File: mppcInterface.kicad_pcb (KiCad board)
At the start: 2 copper layers, 65 x 56.5 mm, 110 parts, among them J1 Conn_Coaxial, J2 Conn_Coaxial, J3 Conn_Coaxial, J4 Conn_Coaxial, J5 Conn_Coaxial, J6 Conn_Coaxial, J7 Conn_Coaxial, J8 Conn_Coaxial, J9 Raspberry_Pi_2_3, Q1 BSS123L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

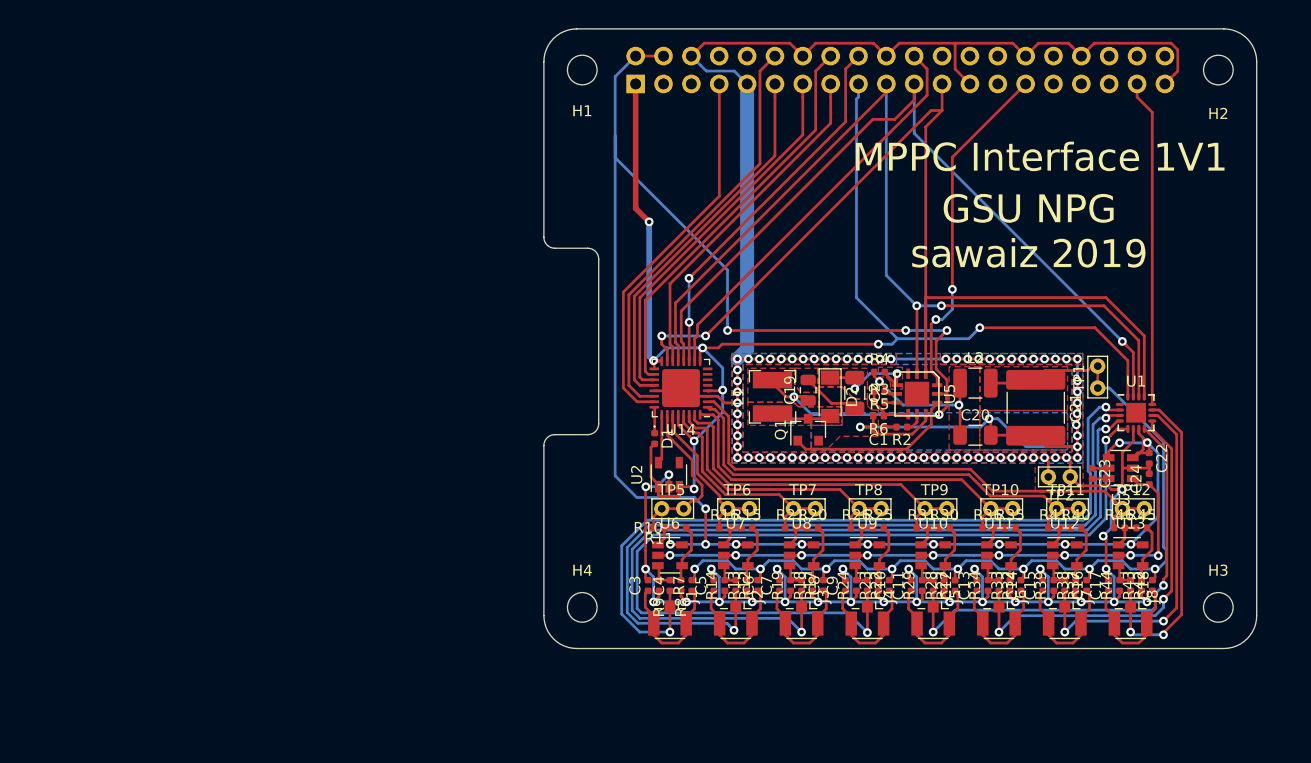
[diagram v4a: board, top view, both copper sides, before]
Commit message: Changed inverter IC, added some decoupling
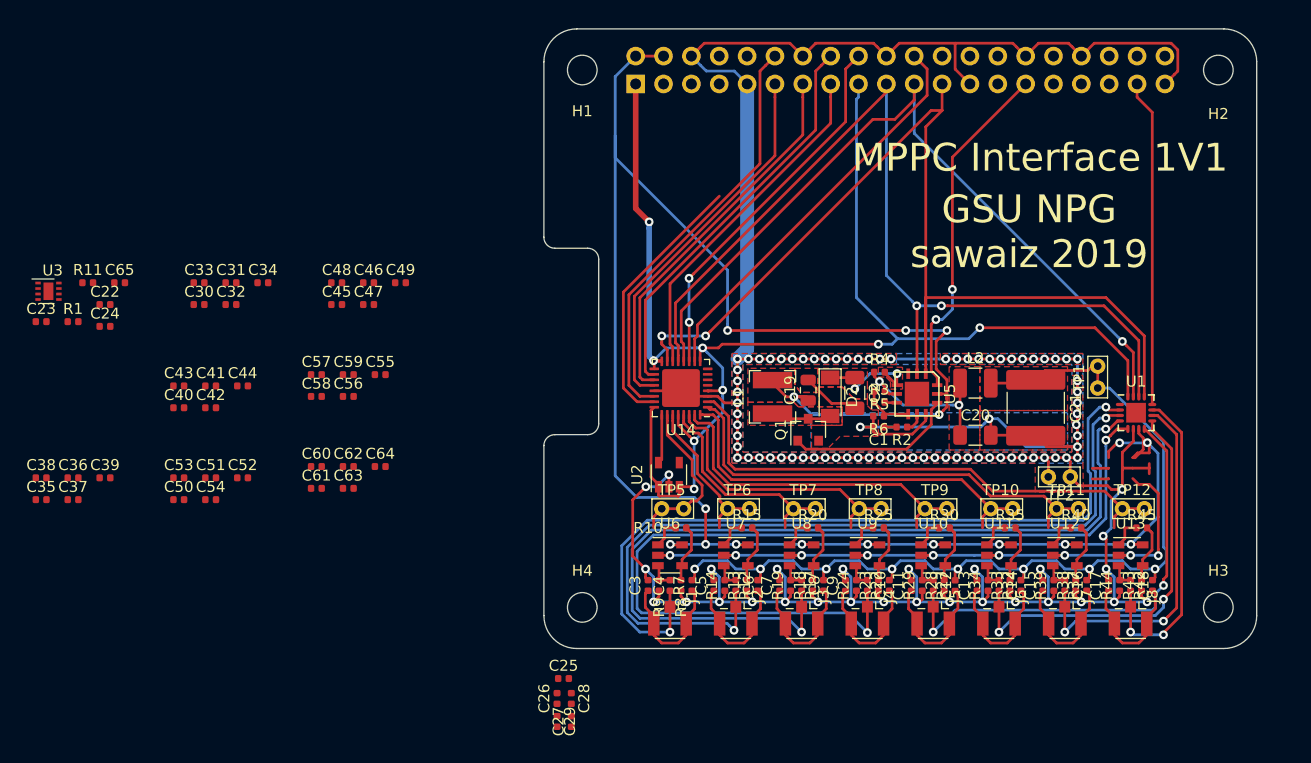
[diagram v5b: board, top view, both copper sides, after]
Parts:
- removed D1: D, Diode_SMD:D_0402_1005Metric
- removed R16, R21, R26, R31, R36, R41, R46: 51R, Resistor_SMD:R_0402_1005Metric
- added C25: 1u, Capacitor_SMD:C_0402_1005Metric, F.Cu at (-30.7, 31.0)
- added C26: 1u, Capacitor_SMD:C_0402_1005Metric, F.Cu at (-31.3, 32.8)
- added C27: 1u, Capacitor_SMD:C_0402_1005Metric, F.Cu at (-30.0, 34.9)
- added C28: 0u1, Capacitor_SMD:C_0402_1005Metric, F.Cu at (-30.0, 32.8)
- added C29: 0u1, Capacitor_SMD:C_0402_1005Metric, F.Cu at (-31.3, 34.9)
- added C30: 1u, Capacitor_SMD:C_0402_1005Metric, F.Cu at (-63.9, -3.11)
- added C31: 1u, Capacitor_SMD:C_0402_1005Metric, F.Cu at (-61.0, -5.10)
- added C32: 1u, Capacitor_SMD:C_0402_1005Metric, F.Cu at (-61.0, -3.11)
- added C33: 0u1, Capacitor_SMD:C_0402_1005Metric, F.Cu at (-63.9, -5.10)
- added C34: 0u1, Capacitor_SMD:C_0402_1005Metric, F.Cu at (-58.1, -5.10)
- added C35: 1u, Capacitor_SMD:C_0402_1005Metric, F.Cu at (-78.3, 14.7)
- added C36: 1u, Capacitor_SMD:C_0402_1005Metric, F.Cu at (-75.4, 12.7)
- added C37: 1u, Capacitor_SMD:C_0402_1005Metric, F.Cu at (-75.4, 14.7)
- added C38: 0u1, Capacitor_SMD:C_0402_1005Metric, F.Cu at (-78.3, 12.7)
- added C39: 0u1, Capacitor_SMD:C_0402_1005Metric, F.Cu at (-72.5, 12.7)
- added C40: 1u, Capacitor_SMD:C_0402_1005Metric, F.Cu at (-65.8, 6.30)
- added C41: 1u, Capacitor_SMD:C_0402_1005Metric, F.Cu at (-62.9, 4.31)
- added C42: 1u, Capacitor_SMD:C_0402_1005Metric, F.Cu at (-62.9, 6.30)
- added C43: 0u1, Capacitor_SMD:C_0402_1005Metric, F.Cu at (-65.8, 4.31)
- added C44: 0u1, Capacitor_SMD:C_0402_1005Metric, F.Cu at (-60.0, 4.31)
- added C45: 1u, Capacitor_SMD:C_0402_1005Metric, F.Cu at (-51.4, -3.11)
- added C46: 1u, Capacitor_SMD:C_0402_1005Metric, F.Cu at (-48.5, -5.10)
- added C47: 1u, Capacitor_SMD:C_0402_1005Metric, F.Cu at (-48.5, -3.11)
- added C48: 0u1, Capacitor_SMD:C_0402_1005Metric, F.Cu at (-51.4, -5.10)
- added C49: 0u1, Capacitor_SMD:C_0402_1005Metric, F.Cu at (-45.6, -5.10)
- added C50: 1u, Capacitor_SMD:C_0402_1005Metric, F.Cu at (-65.8, 14.7)
- added C51: 1u, Capacitor_SMD:C_0402_1005Metric, F.Cu at (-62.9, 12.7)
- added C52: 1u, Capacitor_SMD:C_0402_1005Metric, F.Cu at (-60.0, 12.7)
- added C53: 0u1, Capacitor_SMD:C_0402_1005Metric, F.Cu at (-65.8, 12.7)
- added C54: 0u1, Capacitor_SMD:C_0402_1005Metric, F.Cu at (-62.9, 14.7)
- added C55: 1u, Capacitor_SMD:C_0402_1005Metric, F.Cu at (-47.4, 3.28)
- added C56: 1u, Capacitor_SMD:C_0402_1005Metric, F.Cu at (-50.3, 5.27)
- added C57: 1u, Capacitor_SMD:C_0402_1005Metric, F.Cu at (-53.2, 3.28)
- added C58: 0u1, Capacitor_SMD:C_0402_1005Metric, F.Cu at (-53.2, 5.27)
- added C59: 0u1, Capacitor_SMD:C_0402_1005Metric, F.Cu at (-50.3, 3.28)
- added C60: 1u, Capacitor_SMD:C_0402_1005Metric, F.Cu at (-53.2, 11.7)
- added C61: 1u, Capacitor_SMD:C_0402_1005Metric, F.Cu at (-53.2, 13.6)
- added C62: 1u, Capacitor_SMD:C_0402_1005Metric, F.Cu at (-50.3, 11.7)
- added C63: 0u1, Capacitor_SMD:C_0402_1005Metric, F.Cu at (-50.3, 13.6)
- added C64: 0u1, Capacitor_SMD:C_0402_1005Metric, F.Cu at (-47.4, 11.7)
- added C65: 3u3, Capacitor_SMD:C_0402_1005Metric, F.Cu at (-71.2, -5.10)
- added R1: 1M13, Resistor_SMD:R_0402_1005Metric, F.Cu at (-75.4, -1.55)
- R11: value 51R -> 499k
- R13, R14, R18, R19, R23, R24, R28, R29, R33, R34, R38, R39, R43, R44, R8, R9: value 51R -> 49R9
- U3: value LM2776 -> LM27761; footprint Package_TO_SOT_SMD:SOT-23-6 -> Package_SON:WSON-8-1EP_2x2mm_P0.5mm_EP0.9x1.6mm
- moved U3 99.1 mm to (-77.7, -4.32), turned to 0 degrees
- moved C23 96.8 mm to (-78.3, -1.55), turned to 0 degrees
- moved C22 96.3 mm to (-72.5, -3.11), turned to 0 degrees
- moved C24 96.2 mm to (-72.5, -1.12), turned to 0 degrees
- moved R11 56.7 mm to (-74.1, -5.10)
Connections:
- C24 pad 1: -5V -> Net-(C24-Pad1)
- R10 pad 1: Net-(R10-Pad1) -> Net-(C25-Pad2)
- R11 pad 1: CH0 -> Net-(R1-Pad2)
- R11 pad 2: Net-(R10-Pad1) -> GND
- U14 pad 24: Net-(D1-Pad1) -> +3V3
- U3 pad 1: -5V -> +5V
- U3 pad 3: +5V -> Net-(C24-Pad1)
- U3 pad 4: +5V -> +4V
- U3 pad 5: Net-(C23-Pad1) -> Net-(R1-Pad2)
- U3 pad 6: Net-(C23-Pad2) -> +5V
- U6 pad 1: Net-(R10-Pad1) -> Net-(C25-Pad2)
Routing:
- net CLK: track 34.7 -> 24.5 mm
- net +3V3: track 131.6 -> 134.9 mm
- net Net-(R10-Pad1): track 2.82 -> 0.00 mm
- net Net-(C25-Pad2): track 0.00 -> 2.82 mm
- net Net-(D1-Pad1): track 2.38 -> 0.00 mm
- net GND: track 360.0 -> 360.9 mm

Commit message: Finsihed layout for 1v2
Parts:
- removed C36, C37, C41, C42, C46, C47, C51, C52, C56, C57, C61, C62: 1u, Capacitor_SMD:C_0402_1005Metric
- added J10: RJ14, Connector_RJ:RJ12_Amphenol_54601, F.Cu at (-15.2, -17.1)
- added J11: Conn_02x05_Counter_Clockwise, Connector_PinHeader_2.54mm:PinHeader_2x05_P2.54mm_Vertical_SMD, F.Cu at (6.80, -9.00)
- added J12: RJ45, Connector_RJ:RJ45_Amphenol_54602-x08_Horizontal, F.Cu at (18.0, -8.80)
- added U4: 74HC595, Package_SO:TSSOP-16_4.4x5mm_P0.65mm, F.Cu at (7.40, -18.2)
- moved C23 101.3 mm to (21.8, 13.7), turned to 180 degrees
- moved U3 99.9 mm to (21.0, 11.6), turned to 270 degrees
- moved C22 97.8 mm to (24.1, 12.0), turned to 270 degrees
- moved R1 95.6 mm to (19.2, 11.8), turned to 270 degrees
- moved R11 94.6 mm to (18.8, 13.2), turned to 180 degrees
- moved C24 93.9 mm to (20.8, 9.40)
- moved C65 90.9 mm to (18.1, 11.8), turned to 270 degrees
- moved C53 77.9 mm to (12.0, 17.2), turned to 180 degrees
- moved C50 73.8 mm to (8.00, 17.2)
- moved C60 73.5 mm to (20.0, 17.2)
- moved C63 73.4 mm to (23.0, 12.0), turned to 270 degrees
- moved C38 72.5 mm to (-6.00, 17.2), turned to 180 degrees
- moved C58 72.2 mm to (18.0, 17.2), turned to 180 degrees
- moved C31 70.7 mm to (6.50, 15.8), turned to 90 degrees
- moved C54 69.1 mm to (6.00, 19.8)
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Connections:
- C27 pad 1: -5V -> -4V
- C29 pad 2: -5V -> -4V
- C31 pad 1: GND -> +5V
- C31 pad 2: +5V -> GND
- C32 pad 1: -5V -> GND
- C32 pad 2: GND -> -4V
- C34 pad 2: -5V -> -4V
- C39 pad 2: -5V -> -4V
- C44 pad 2: -5V -> -4V
- C49 pad 2: -5V -> -4V
- C54 pad 2: -5V -> -4V
- C59 pad 2: -5V -> -4V
- C64 pad 2: -5V -> -4V
- C65 pad 1: +4V -> -4V
- J9 pad 15: FPGA_CS -> Net-(J9-Pad15)
- J9 pad 29: HV_CS -> Net-(J9-Pad29)
- J9 pad 33: Net-(J9-Pad33) -> SRDATA
- J9 pad 36: Net-(J9-Pad36) -> RCLK
- J9 pad 37: DAC_CS -> SRCLK
- J9 pad 5: SDL -> SCL
- R1 pad 1: +4V -> -4V
- U10 pad 2: -5V -> -4V
- U11 pad 2: -5V -> -4V
- U12 pad 2: -5V -> -4V
- U13 pad 2: -5V -> -4V
- U3 pad 4: +4V -> -4V
- U6 pad 2: -5V -> -4V
- U7 pad 2: -5V -> -4V
- U8 pad 2: -5V -> -4V
- U9 pad 2: -5V -> -4V
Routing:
- net -4V: track 0.00 -> 85.2 mm, vias 0 -> 10
- net GND: track 360.9 -> 441.6 mm
- net -5V: track 61.9 -> 0.00 mm, vias 9 -> 0
- net +3V3: track 134.9 -> 190.7 mm, vias 8 -> 14
- net CLK: track 24.5 -> 56.0 mm
- net MISO: track 72.1 -> 93.2 mm, vias 1 -> 4
- net RCLK: track 0.00 -> 21.0 mm, vias 0 -> 1
- net SRCLK: track 0.00 -> 20.2 mm, vias 0 -> 1
- net GPIO18: track 38.3 -> 55.6 mm
- net GPIO17: track 34.3 -> 50.5 mm
- net FPGA_RST: track 37.1 -> 52.7 mm, vias 0 -> 4
- net FPGA_DONE: track 34.2 -> 49.5 mm
- net FPGA_CS: track 31.5 -> 46.3 mm, vias 0 -> 4
- net SPI_EX4: track 0.00 -> 14.6 mm
- net GPIO27: track 34.3 -> 48.3 mm
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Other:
- outline, holes or cut-outs redrawn
- board text added: "MPPC Interface 1V2"
- board text removed: "MPPC Interface 1V1"
- board text removed: "PROJ = coincidence BUILD = ./build DEVICE = 384 FOOTPRINT = qn32 FILES = top.v .PHONY: all clean burn all: mkdir -p $(BUILD) # synthesize using Yosys yosys -p "synth_ice40 -top top -blif $(BUILD)/$(PROJ).blif" $(FILES) # Place and route using arachne arachne-pnr -d $(DEVICE) -P $(FOOTPRINT) -o $(BUILD)/$(PROJ).asc -p pinmap.pcf $(BUILD)/$(PROJ).blif # Convert to bitstream using IcePack icepack $(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"

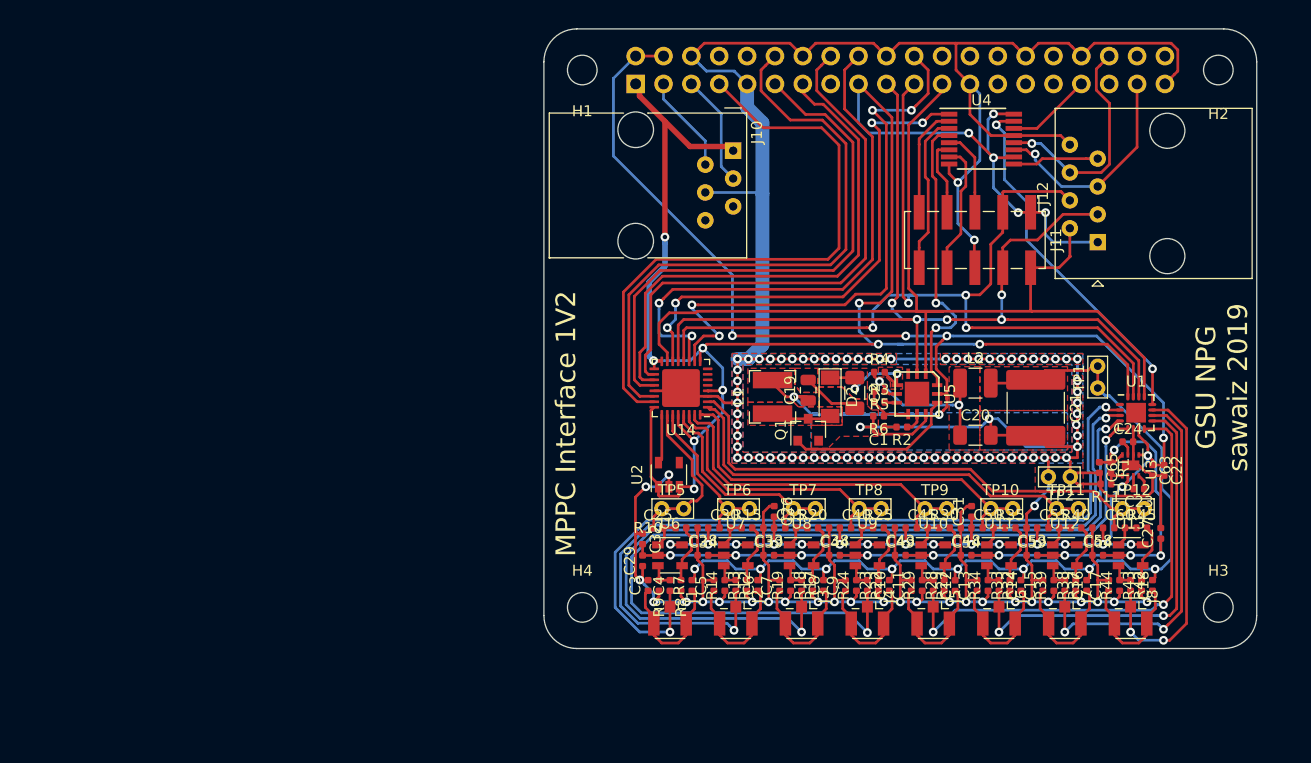
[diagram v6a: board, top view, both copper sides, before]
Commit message: Added more decopling, changed I2C jack to be compatible with 6P4C
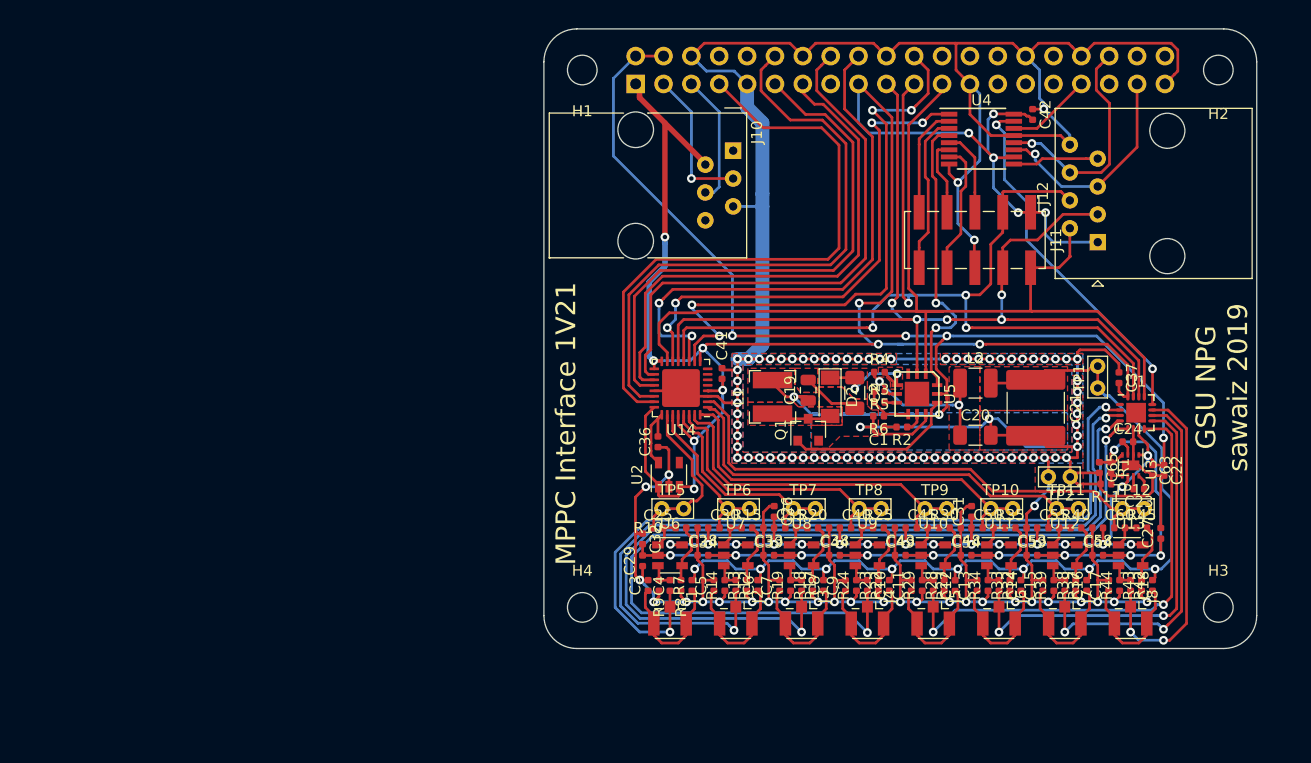
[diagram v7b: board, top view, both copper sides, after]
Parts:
- added C36: 1u, Capacitor_SMD:C_0402_1005Metric, F.Cu at (-22.1, 9.40)
- added C37: 1u, Capacitor_SMD:C_0402_1005Metric, F.Cu at (19.9, 3.56)
- added C41: 1u, Capacitor_SMD:C_0402_1005Metric, F.Cu at (-16.3, 3.17)
- added C42: 1u, Capacitor_SMD:C_0402_1005Metric, F.Cu at (12.1, -20.4)
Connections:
- J10 pad 1: +3V3 -> Net-(J10-Pad1)
- J10 pad 2: SDA -> +3V3
- J10 pad 3: SCL -> SDA
- J10 pad 4: GND -> SCL
- J10 pad 5: (no net) -> GND
- J10 pad 6: (no net) -> Net-(J10-Pad6)
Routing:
- net GND: track 441.6 -> 460.6 mm, vias 105 -> 106
- net SDA: track 8.93 -> 13.5 mm, vias 0 -> 1
- net +3V3: track 190.7 -> 193.9 mm
- net +1V2: track 4.49 -> 7.18 mm
- net SCL: track 10.2 -> 11.9 mm
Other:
- board text added: "MPPC Interface 1V21"
- board text removed: "MPPC Interface 1V2"
